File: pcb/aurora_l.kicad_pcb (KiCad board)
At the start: 2 copper layers, 118 x 114.2 mm, 92 parts

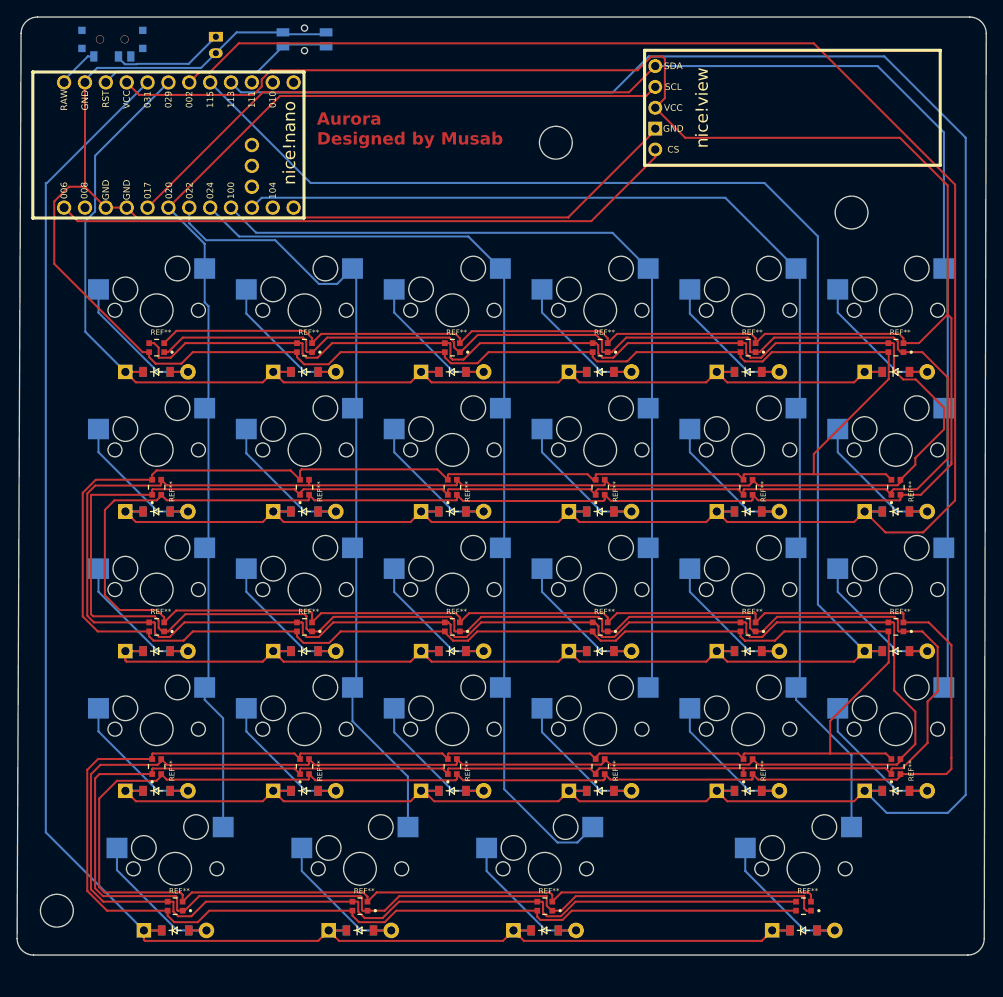
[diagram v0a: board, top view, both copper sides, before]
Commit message: Add stab holes and extended base to PCB
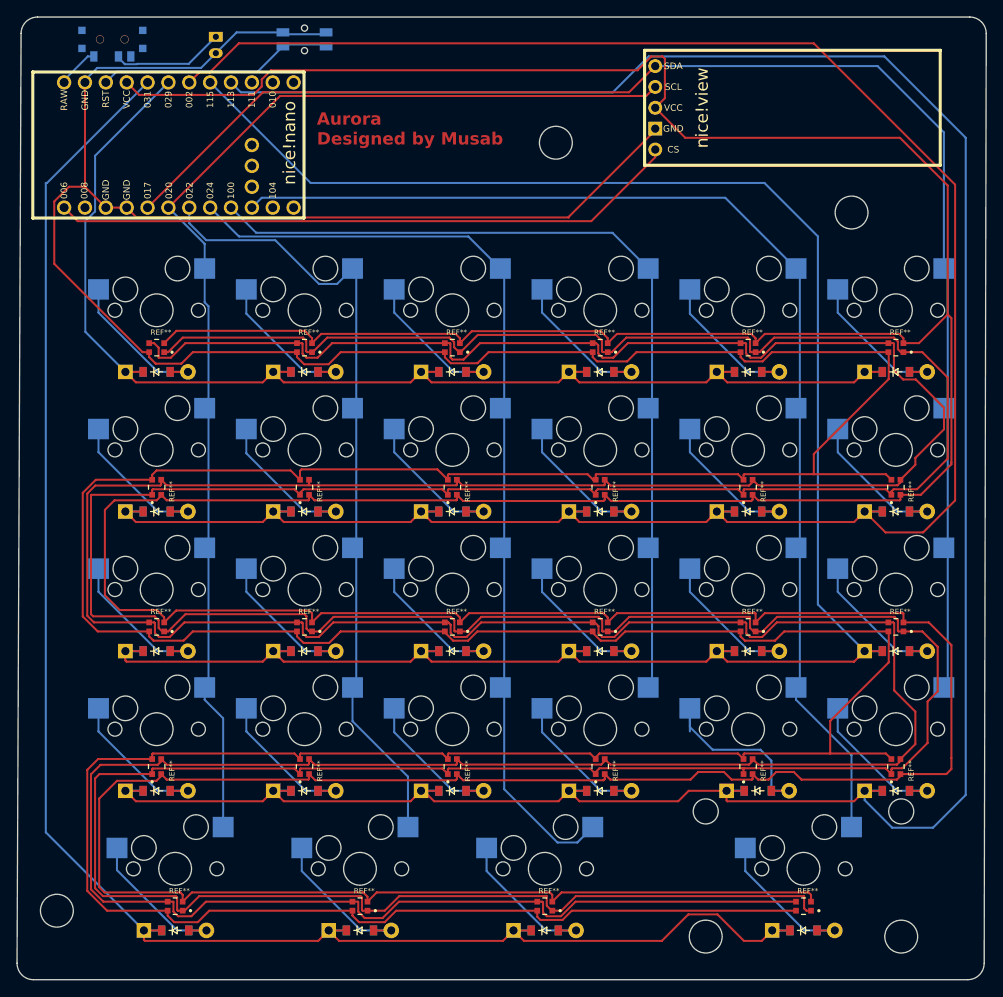
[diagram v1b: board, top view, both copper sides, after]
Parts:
- added REF**: SW_Cherry_MX_2.25u_PCB, Button_Switch_Keyboard:SW_Cherry_MX_2.25u_PCB, F.Cu at (136.3, 185.9)
- moved D17 1.19 mm to (128.2, 181.5)
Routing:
- net five_bottom: track 18.9 -> 24.7 mm
- net P113: track 311.4 -> 314.3 mm
- net P031: track 211.0 -> 213.7 mm
- net VCC: track 714.4 -> 716.0 mm
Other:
- board size 118 x 114.2 mm -> 118 x 117.2 mm

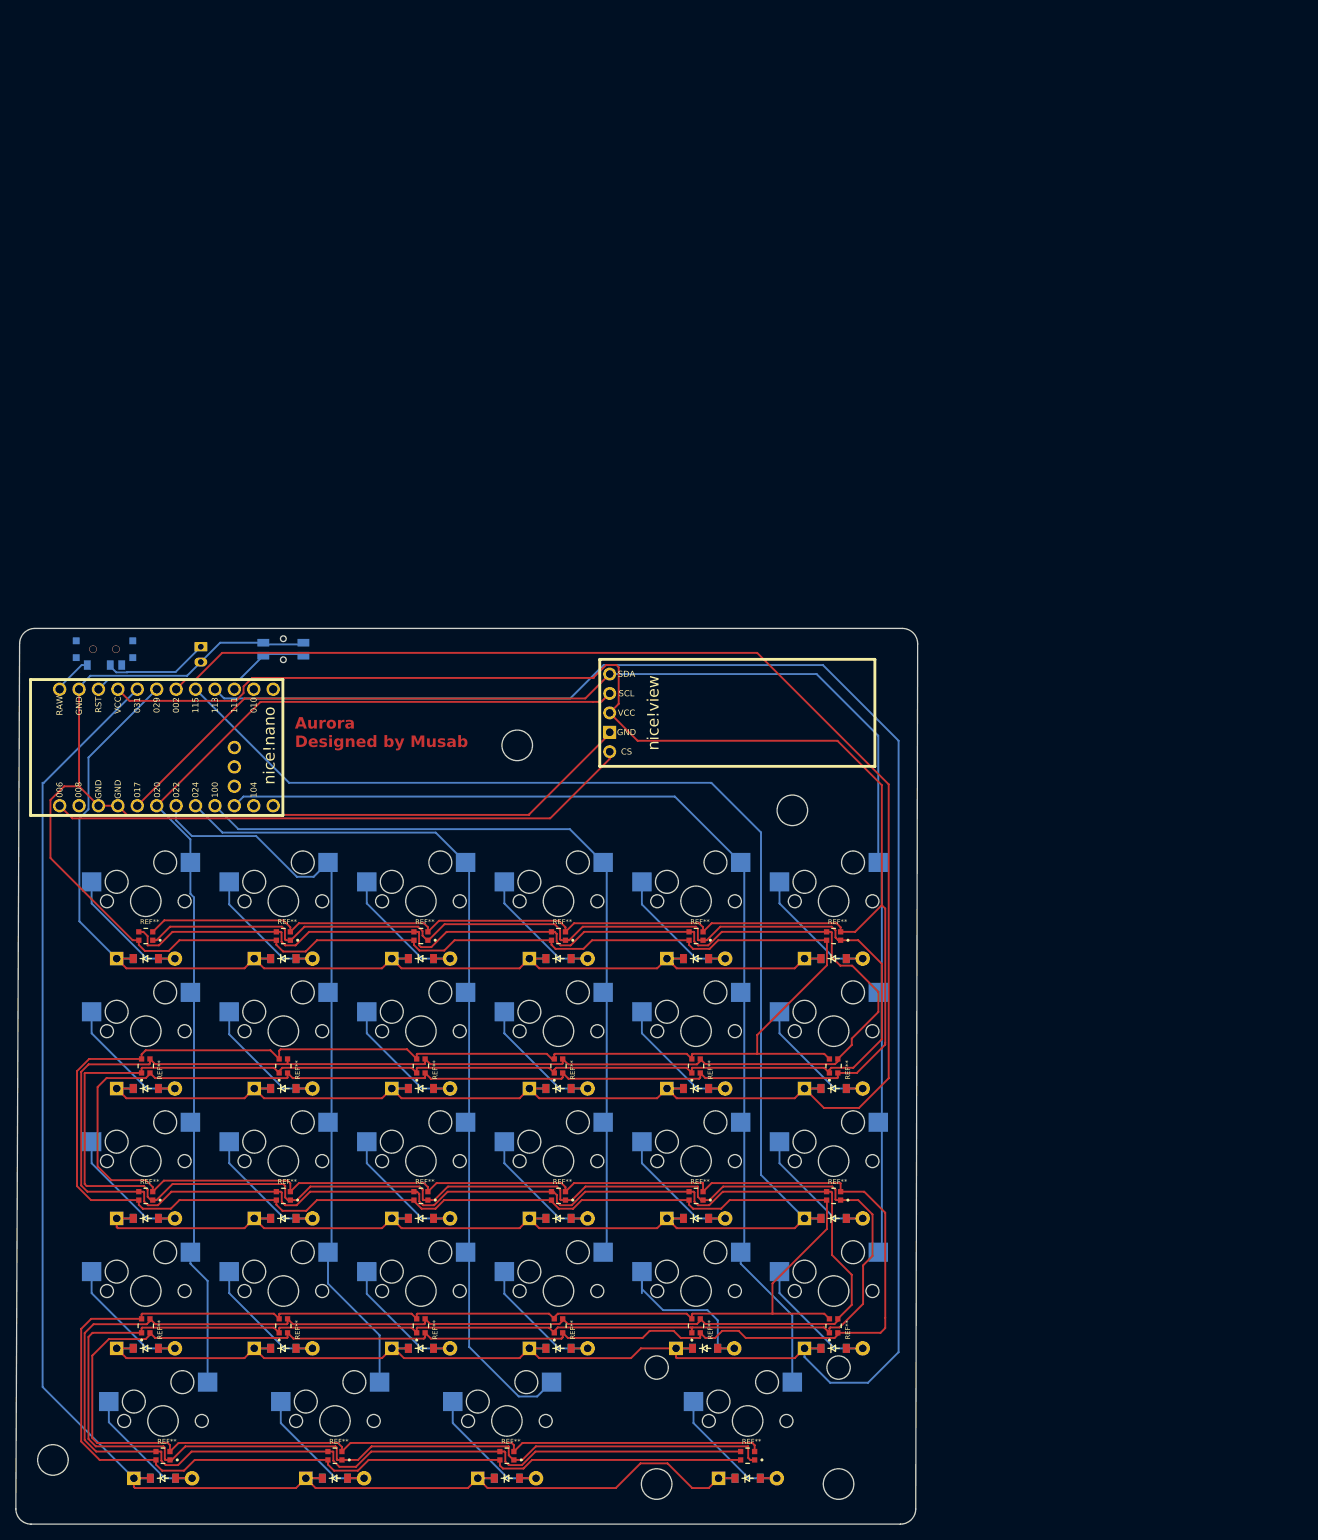
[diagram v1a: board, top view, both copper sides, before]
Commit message: Fixed left PCBs with routing
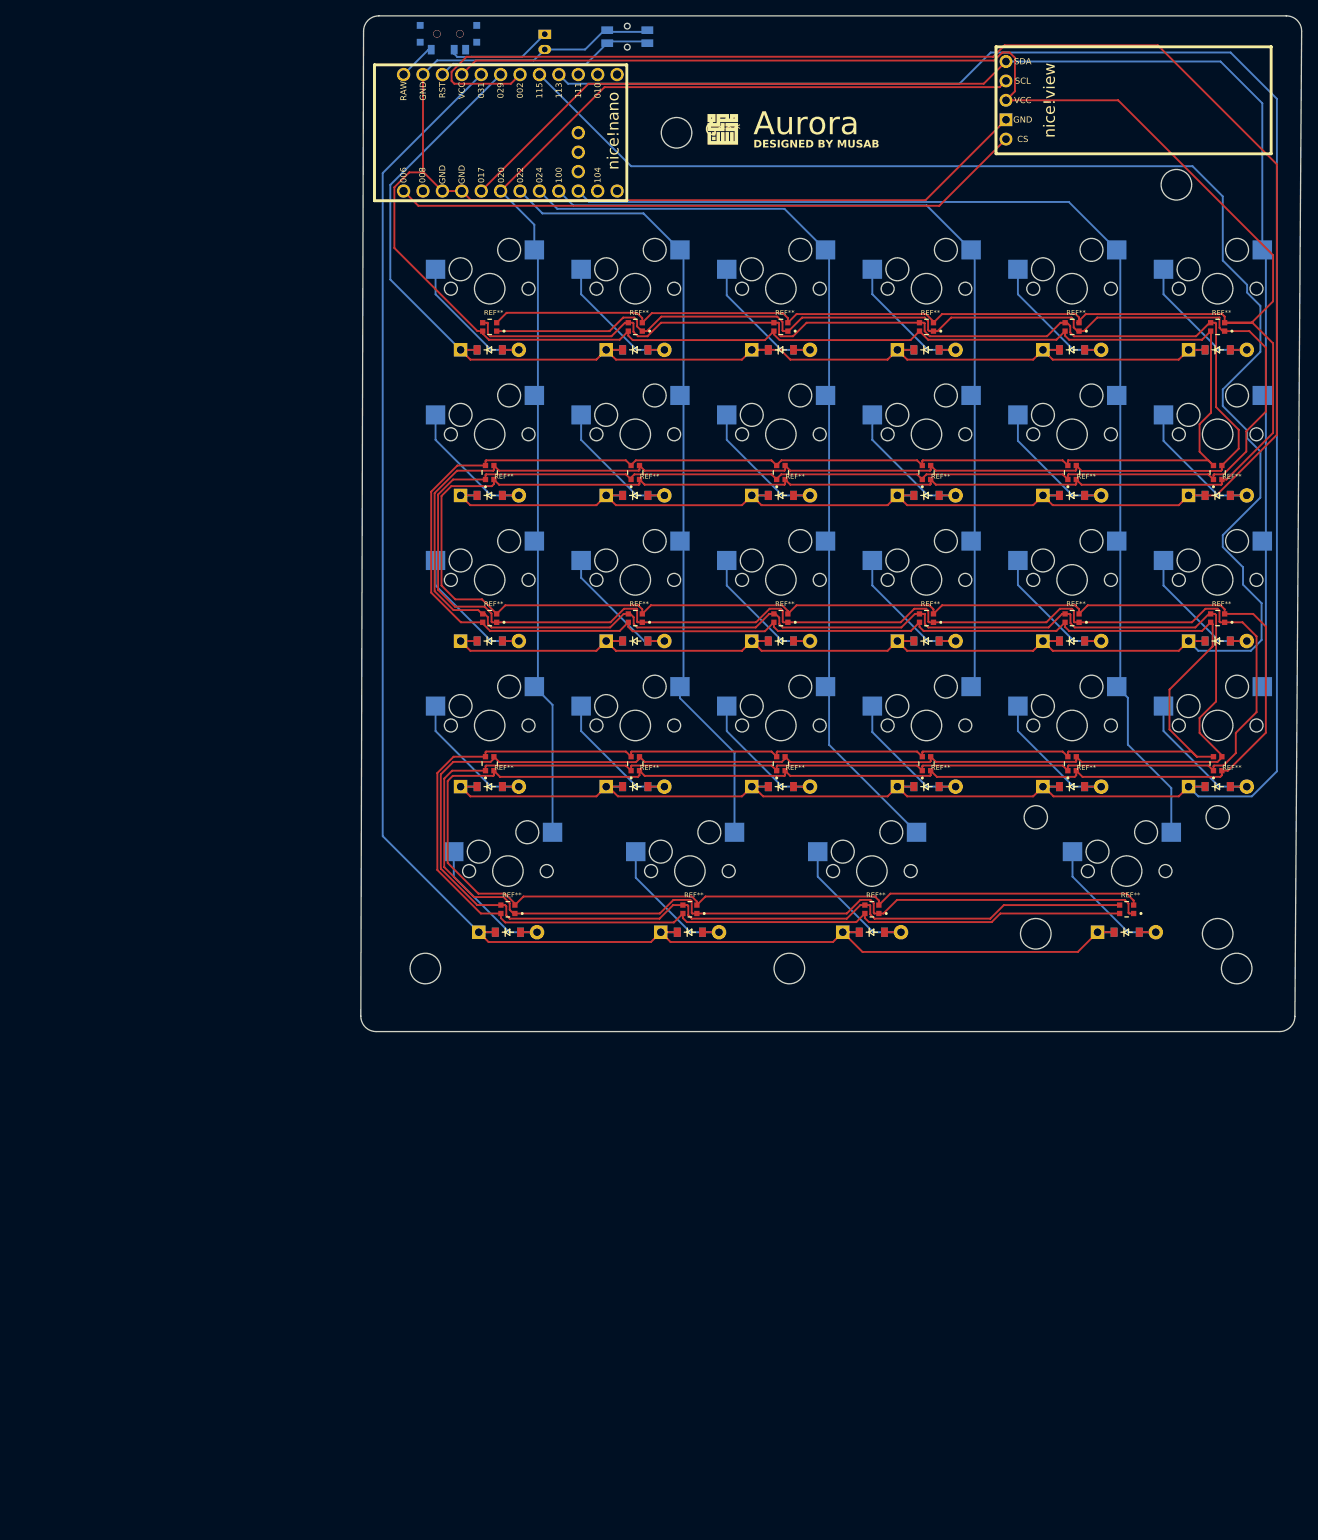
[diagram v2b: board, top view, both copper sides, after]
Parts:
- removed the ? at (103.6, 102.6)
- removed the ? at (42.9, 196.1)
- removed the ? at (139.6, 111.1)
- removed the REF** at (109.0, 178.6)
- removed the REF** at (79.8, 195.6)
- removed the REF** at (109.0, 144.6)
- removed the REF** at (127.0, 144.6)
- removed the REF** at (55.0, 144.6)
- removed the REF** at (145.0, 178.6)
- removed the REF** at (127.0, 178.6)
- removed the REF** at (57.2, 195.6)
- removed the REF** at (55.0, 161.6)
- removed the REF** at (133.8, 195.6)
- removed the REF** at (91.0, 144.6)
- removed the REF** at (91.0, 127.5)
- removed the REF** at (91.0, 161.6)
- removed the REF** at (73.0, 178.6)
- removed the REF** at (127.0, 161.6)
- removed the REF** at (145.0, 127.5)
- removed the REF** at (73.0, 127.5)
- removed the REF** at (127.0, 127.5)
- removed the REF** at (145.0, 144.6)
- removed the REF** at (91.0, 178.6)
- removed the REF** at (55.0, 178.6)
- removed the REF** at (109.0, 161.6)
- removed the REF** at (55.0, 127.5)
- removed the REF** at (109.0, 127.5)
- removed the REF** at (73.0, 161.6)
- removed the REF** at (145.0, 161.6)
- removed the REF** at (73.0, 144.6)
- removed the REF** at (102.2, 195.6)
- added ?: , HOLE_M2_TH, F.Cu at (139.2, 131.8)
- added ?: , HOLE_M2_TH, F.Cu at (91.6, 131.8)
- added ?: , HOLE_M2_TH, F.Cu at (124.5, 22.4)
- added ?: , HOLE_M2_TH, F.Cu at (197.7, 131.8)
- added ?: , HOLE_M2_TH, F.Cu at (189.8, 29.2)
- added G***: LOGO, Logos:PCB_footprint, F.Cu at (130.5, 22.0)
- added REF**: WS2812, WS2812-2020, F.Cu at (102.4, 124.0)
- added REF**: WS2812, WS2812-2020, F.Cu at (176.2, 86.0)
- added REF**: WS2812, WS2812-2020, F.Cu at (138.1, 105.0)
- added REF**: WS2812, WS2812-2020, F.Cu at (100.0, 86.0)
- added REF**: WS2812, WS2812-2020, F.Cu at (195.2, 47.9)
- added REF**: WS2812, WS2812-2020, F.Cu at (119.0, 86.0)
- added REF**: WS2812, WS2812-2020, F.Cu at (119.0, 47.9)
- added REF**: WS2812, WS2812-2020, F.Cu at (195.2, 66.9)
- added REF**: WS2812, WS2812-2020, F.Cu at (119.0, 105.0)
- added REF**: WS2812, WS2812-2020, F.Cu at (100.0, 47.9)
- added REF**: WS2812, WS2812-2020, F.Cu at (100.0, 66.9)
- added REF**: WS2812, WS2812-2020, F.Cu at (138.1, 86.0)
- added REF**: WS2812, WS2812-2020, F.Cu at (183.3, 124.0)
- added REF**: WS2812, WS2812-2020, F.Cu at (195.2, 86.0)
- added REF**: WS2812, WS2812-2020, F.Cu at (138.1, 47.9)
- added REF**: WS2812, WS2812-2020, F.Cu at (157.2, 86.0)
- added REF**: WS2812, WS2812-2020, F.Cu at (157.2, 47.9)
- added REF**: WS2812, WS2812-2020, F.Cu at (157.2, 66.9)
- added REF**: WS2812, WS2812-2020, F.Cu at (100.0, 105.0)
- added REF**: WS2812, WS2812-2020, F.Cu at (126.2, 124.0)
- added REF**: WS2812, WS2812-2020, F.Cu at (195.2, 105.0)
- added REF**: WS2812, WS2812-2020, F.Cu at (176.2, 66.9)
- added REF**: WS2812, WS2812-2020, F.Cu at (119.0, 66.9)
- added REF**: WS2812, WS2812-2020, F.Cu at (176.2, 47.9)
- added REF**: WS2812, WS2812-2020, F.Cu at (150.0, 124.0)
- added REF**: WS2812, WS2812-2020, F.Cu at (138.1, 66.9)
- added REF**: WS2812, WS2812-2020, F.Cu at (176.2, 105.0)
- added REF**: WS2812, WS2812-2020, F.Cu at (157.2, 105.0)
- moved niceView1 95.5 mm to (166.2, 18.2)
- moved S24 94.6 mm to (195.2, 42.9)
- moved D24 94.2 mm to (195.2, 50.9)
- moved S20 94.0 mm to (176.2, 42.9)
- moved D20 93.6 mm to (176.2, 50.9)
- moved S16 93.5 mm to (157.2, 42.9)
- moved D16 93.1 mm to (157.2, 50.9)
- moved S12 93.0 mm to (138.1, 42.9)
- moved S23 92.9 mm to (195.2, 61.9)
- moved D12 92.5 mm to (138.1, 50.9)
- moved D23 92.4 mm to (195.2, 69.9)
- moved S8 92.4 mm to (119.0, 42.9)
- moved S19 92.3 mm to (176.2, 61.9)
- moved T1 92.2 mm to (94.6, 9.50)
- moved MCU1 92.2 mm to (102.7, 22.4)
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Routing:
- net P115: track 256.5 -> 301.5 mm
- net GND: track 715.9 -> 743.0 mm
- net P002: track 275.7 -> 301.2 mm
- net VCC: track 716.0 -> 739.3 mm
- net P8: track 588.7 -> 611.2 mm
- net P15: track 581.2 -> 601.1 mm
- net P020: track 144.7 -> 160.0 mm
- net P017: track 176.2 -> 189.0 mm
- net P113: track 314.3 -> 326.6 mm
- net P011: track 142.3 -> 154.0 mm
- net P031: track 213.7 -> 225.3 mm
- net P029: track 162.7 -> 172.3 mm
- net P100: track 106.0 -> 115.4 mm
- net P022: track 97.6 -> 104.4 mm
- net P006: track 76.8 -> 83.2 mm
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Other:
- board size 118 x 117.2 mm -> 123.1 x 132.9 mm
- board text added: "Aurora"
- board text added: "DESIGNED BY MUSAB"
- board text removed: "Aurora Designed by Musab"

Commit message: Left PCB pin layout fixes and full routed pcb
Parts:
- removed the ? at (139.2, 131.8)
- removed the ? at (91.6, 131.8)
- removed the ? at (124.5, 22.4)
- removed the ? at (197.7, 131.8)
- removed the ? at (189.8, 29.2)
- removed the REF** at (185.9, 113.9)
- added ?: , HOLE_M2_TH, F.Cu at (185.7, 52.4)
- added ?: , HOLE_M2_TH, F.Cu at (109.5, 90.5)
- added ?: , HOLE_M2_TH, F.Cu at (109.5, 52.4)
- added ?: , HOLE_M2_TH, F.Cu at (185.7, 90.5)
- moved niceView1 117.7 mm to (73.3, 90.5), turned to -90 degrees
- moved T1 86.8 mm to (63.4, 90.5), turned to 90 degrees
- moved B1 78.8 mm to (63.4, 66.7), turned to 90 degrees
- moved JST1 77.7 mm to (65.7, 76.2), turned to 0 degrees
- moved G*** 76.9 mm to (68.5, 67.5)
- moved MCU1 36.0 mm to (75.2, 45.7), turned to -90 degrees
- moved D25 2.00 mm to (102.4, 129.1)
- moved D26 2.00 mm to (126.2, 129.1)
- moved D27 2.00 mm to (150.0, 129.1)
- moved D28 2.00 mm to (183.3, 129.1)
- moved D1 2.00 mm to (100.0, 110.0)
- moved D10 2.00 mm to (138.1, 91.0)
- moved D11 2.00 mm to (138.1, 71.9)
- moved D12 2.00 mm to (138.1, 52.9)
- moved D13 2.00 mm to (157.2, 110.0)
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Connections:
- D1 pad 1: P113 -> P115
- D10 pad 1: P115 -> P002
- D11 pad 1: P002 -> P029
- D12 pad 1: P029 -> P031
- D13 pad 1: P113 -> P115
- D14 pad 1: P115 -> P002
- D15 pad 1: P002 -> P029
- D16 pad 1: P029 -> P031
- D17 pad 1: P113 -> P115
- D18 pad 1: P115 -> P002
- D19 pad 1: P002 -> P029
- D2 pad 1: P115 -> P002
- D20 pad 1: P029 -> P031
- D21 pad 1: P113 -> P115
- D22 pad 1: P115 -> P002
- D23 pad 1: P002 -> P029
- D24 pad 1: P029 -> P031
- D25 pad 1: P031 -> P113
- D26 pad 1: P031 -> P113
- D27 pad 1: P031 -> P113
- D28 pad 1: P031 -> P113
- D3 pad 1: P002 -> P029
- D4 pad 1: P029 -> P031
- D5 pad 1: P113 -> P115
- D6 pad 1: P115 -> P002
- D7 pad 1: P002 -> P029
- D8 pad 1: P029 -> P031
- D9 pad 1: P113 -> P115
- REF** pad 1: P8 -> P010 (x28)
- REF** pad 3: P15 -> P009 (x28)
- S1 pad 2: P020 -> P011
- S13 pad 2: P100 -> P022
- S14 pad 2: P100 -> P022
- S15 pad 2: P100 -> P022
- S16 pad 2: P100 -> P022
- S17 pad 2: P011 -> P020
- S18 pad 2: P011 -> P020
- S19 pad 2: P011 -> P020
- S2 pad 2: P020 -> P011
- S20 pad 2: P011 -> P020
- S25 pad 2: P020 -> P011
- S26 pad 2: P022 -> P100
- S27 pad 2: P024 -> P022
- S28 pad 2: P011 -> P017
- S3 pad 2: P020 -> P011
- S4 pad 2: P020 -> P011
- S5 pad 2: P022 -> P100
- S6 pad 2: P022 -> P100
- S7 pad 2: P022 -> P100
- S8 pad 2: P022 -> P100
- niceView1 pad 1: P006 -> P101
- niceView1 pad 4: P020 -> P102
- niceView1 pad 5: P017 -> P107
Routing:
- net P009: track 0.00 -> 946.9 mm
- net P010: track 0.00 -> 637.9 mm
- net P8: track 611.2 -> 0.00 mm
- net P15: track 601.1 -> 0.00 mm
- net P113: track 326.6 -> 185.1 mm
- net P002: track 301.2 -> 179.0 mm
- net GND: track 743.0 -> 862.9 mm
- net P115: track 301.5 -> 192.5 mm
- net P022: track 104.4 -> 190.3 mm
- net RAW: track 4.97 -> 88.8 mm
- net P006: track 83.2 -> 0.00 mm
- net P031: track 225.3 -> 147.1 mm
- net VCC: track 739.3 -> 675.9 mm
- net P017: track 189.0 -> 229.6 mm
- net P102: track 0.00 -> 38.5 mm
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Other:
- board size 123.1 x 132.9 mm -> 145.1 x 107.7 mm
- board text added: "Designed by Musab"
- board text removed: "DESIGNED BY MUSAB"
